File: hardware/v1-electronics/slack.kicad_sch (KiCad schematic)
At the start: 0 parts

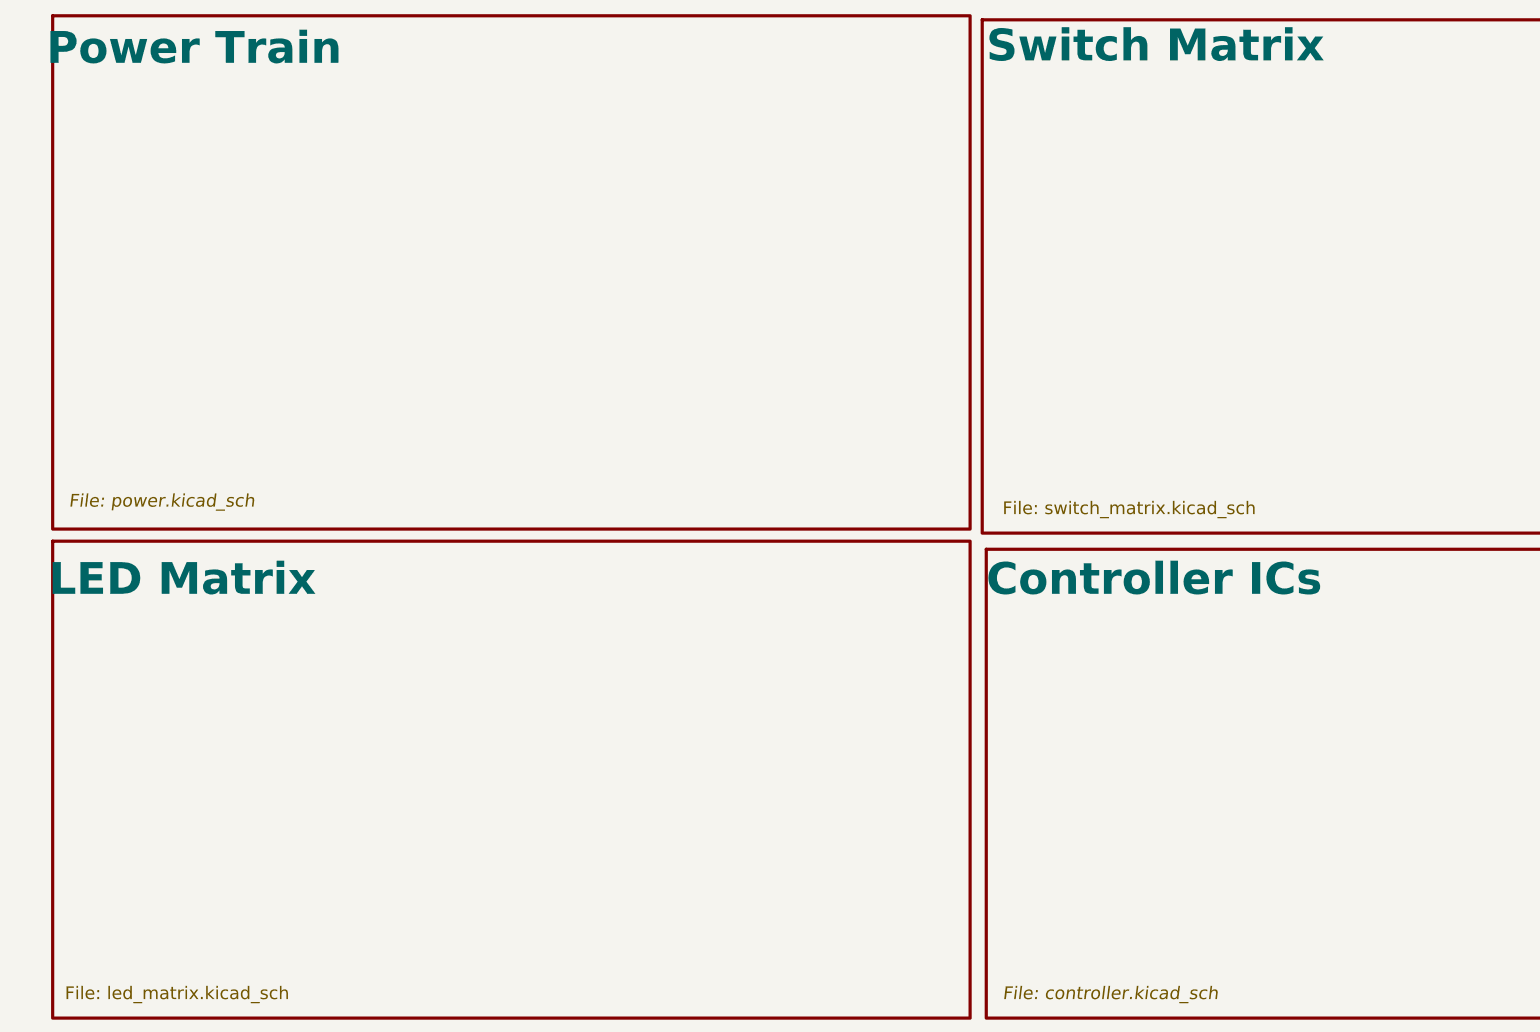
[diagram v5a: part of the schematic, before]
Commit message: feat(v1 hardware): RGBW LED matrix halve 1
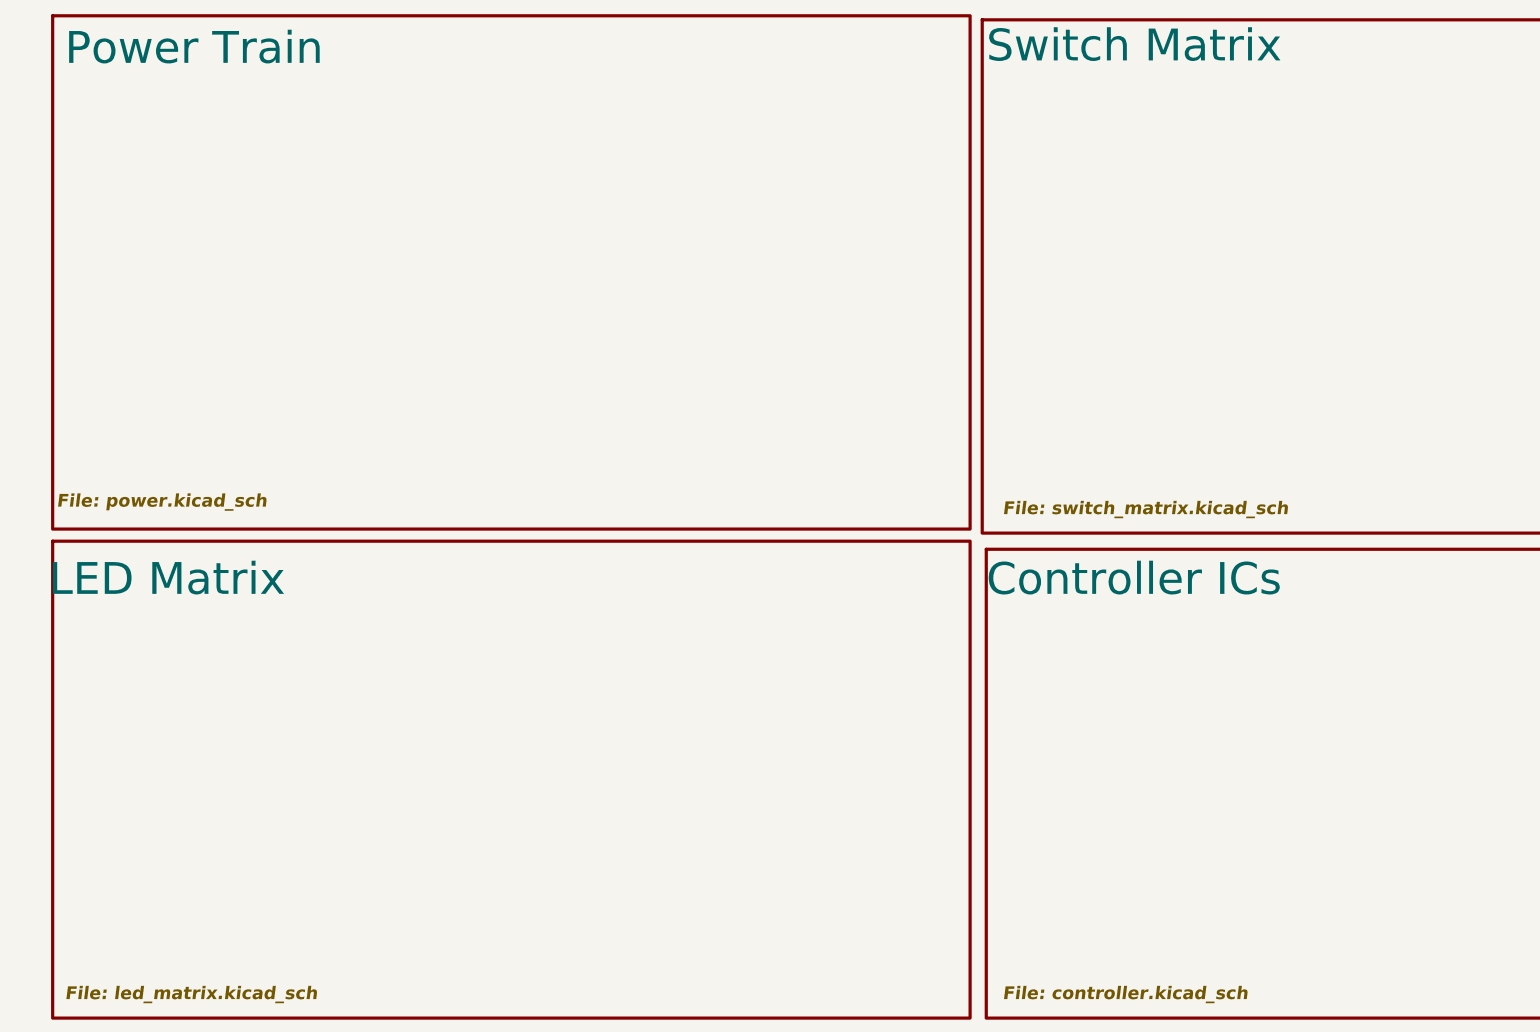
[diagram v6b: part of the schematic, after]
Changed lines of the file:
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@@
 				(font
 					(size 5 5)
-					(thickness 1)
-					(bold yes)
+					(thickness 0.625)
 				)
 				(justify left bottom)
@@
 				(font
 					(size 2 2)
+					(thickness 0.4)
+					(bold yes)
+					(italic yes)
 				)
 				(justify left top)
@@
 				(font
 					(size 5 5)
-					(thickness 0.254)
-					(bold yes)
+					(thickness 0.625)
 				)
 			)
@@
 				(font
 					(size 2 2)
+					(thickness 0.4)
+					(bold yes)
 					(italic yes)
 				)
@@
 				(font
 					(size 5 5)
-					(thickness 0.254)
-					(bold yes)
+					(thickness 0.625)
 				)
 				(justify left bottom)
@@
 				(font
 					(size 2 2)
+					(thickness 0.4)
+					(bold yes)
 					(italic yes)
 				)
@@
 				(font
 					(size 5 5)
-					(thickness 1)
-					(bold yes)
+					(thickness 0.625)
 				)
 				(justify left bottom)
@@
 				(font
 					(size 2 2)
+					(thickness 0.4)
+					(bold yes)
+					(italic yes)
 				)
 				(justify left top)

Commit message: refactor(v1 hardware): add different charger ic & clean-up schematics
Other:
- note added: "- Compare charger ICs - Check circuits - Choose passive conponent values - Connect the LED and Switch matrices. Assign LEDs to each inputs. - Select PCB foot prints"
- note added: "Loose Notes"
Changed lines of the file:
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@@
 	(generator_version "10.0")
 	(paper "A2")
-	(sheet
-		(at 159.385 15.875)
-		(size 145.415 80.645)
+	(rectangle
+		(start 307.34 15.24)
+		(end 431.8 96.52)
+		(stroke
+			(width 0.5)
+			(type default)
+		)
+		(fill
+			(type none)
+		)
+	)
+	(text "Loose Notes"
+		(exclude_from_sim no)
+		(at 309.88 20.32 0)
+		(effects
+			(font
+				(size 5 5)
+				(thickness 0.625)
+			)
+			(justify left top)
+		)
+	)
+	(text "- Compare charger ICs\n- Check circuits\n- Choose passive conponent values\n- Connect the LED and Switch matrices. Assign LEDs to each inputs.\n- Select PCB foot prints"
+		(exclude_from_sim no)
+		(at 312.42 27.94 0)
+		(effects
+			(font
+				(size 1.5 1.5)
+			)
+			(justify left top)
+		)
+	)
+	(sheet
+		(at 160.02 15.24)
+		(size 144.78 81.28)
 		(exclude_from_sim no)
 		(in_bom yes)
@@
 		)
 		(property "Sheetname" "Switch Matrix"
-			(at 160.02 22.86 0)
+			(at 160.655 22.225 0)
 			(show_name no)
 			(do_not_autoplace no)
@@
 		)
 		(property "Sheetfile" "switch_matrix.kicad_sch"
-			(at 162.56 91.44 0)
+			(at 163.195 90.805 0)
 			(show_name no)
 			(do_not_autoplace no)
@@
 	)
 	(sheet
-		(at 13.335 15.24)
-		(size 144.145 80.645)
+		(at 12.7 15.24)
+		(size 144.78 81.28)
 		(exclude_from_sim no)
 		(in_bom yes)
@@
 		)
 		(property "Sheetname" "Power Train"
-			(at 35.56 20.32 0)
+			(at 34.925 20.32 0)
 			(show_name no)
 			(do_not_autoplace no)
@@
 		)
 		(property "Sheetfile" "power.kicad_sch"
-			(at 30.48 91.44 0)
+			(at 29.845 91.44 0)
 			(show_name no)
 			(do_not_autoplace no)
@@
 	)
 	(sheet
-		(at 13.335 97.79)
-		(size 144.145 74.93)
+		(at 12.7 99.06)
+		(size 144.78 73.66)
 		(exclude_from_sim no)
 		(in_bom yes)
@@
 		)
 		(property "Sheetname" "LED Matrix"
-			(at 12.7 106.68 0)
+			(at 12.065 107.95 0)
 			(show_name no)
 			(do_not_autoplace no)
@@
 		)
 		(property "Sheetfile" "led_matrix.kicad_sch"
-			(at 15.24 167.64 0)
-			(show_name no)
-			(do_not_autoplace no)
+			(at 14.605 168.91 0)
+			(show_name no)
+			(do_not_autoplace no)

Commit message: refactor(v1 hardware): convert switch matrix to hierarchical pins
made other changes
had claude generate a script for making the convertion
the references for this file still need to be fixed
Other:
- sheet Power Train ports: added D+, D-, VBUS, V_SYS; removed none
- sheet Switch Matrix ports: added Column 1, Column 10, Column 11, Column 12, Column 13, Column 14, Column 2, Column 3, Column 4, Column 5, Column 6, Column 7, Column 8, Column 9, RE10_A-Channel, RE10_B-Channel, RE1_A-Channel, RE1_B-Channel, RE2_A-Channel, RE2_B-Channel, RE3_A-Channel, RE3_B-Channel, RE4_A-Channel, RE4_B-Channel, RE5_A-Channel, RE5_B-Channel, RE6_A-Channel, RE6_B-Channel, RE7_A-Channel, RE7_B-Channel, RE8_A-Channel, RE8_B-Channel, RE9_A-Channel, RE9_B-Channel, Row 1, Row 2, Row 3, Row 4, Row 5, Row 6; removed none
- note added: "- Compare charger ICs - Check circuits - Choose passive conponent values - Connect the LED and Switch matrices. Assign LEDs to each inputs. - Select PCB foot prints Schematic - Refactor Schematic to r/PrintedCircuitBoard Guide - Refactor the root schematic to show how the system is connected - Refactor chip configurations to explain my choices - Rename all the component references so they are gro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"
- note removed: "- Compare charger ICs - Check circuits - Choose passive conponent values - Connect the LED and Switch matrices. Assign LEDs to each inputs. - Select PCB foot prints"
- title: (none) -> Slack
